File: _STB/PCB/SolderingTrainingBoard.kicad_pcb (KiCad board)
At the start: 2 copper layers, 87.3 x 87.3 mm, 161 parts

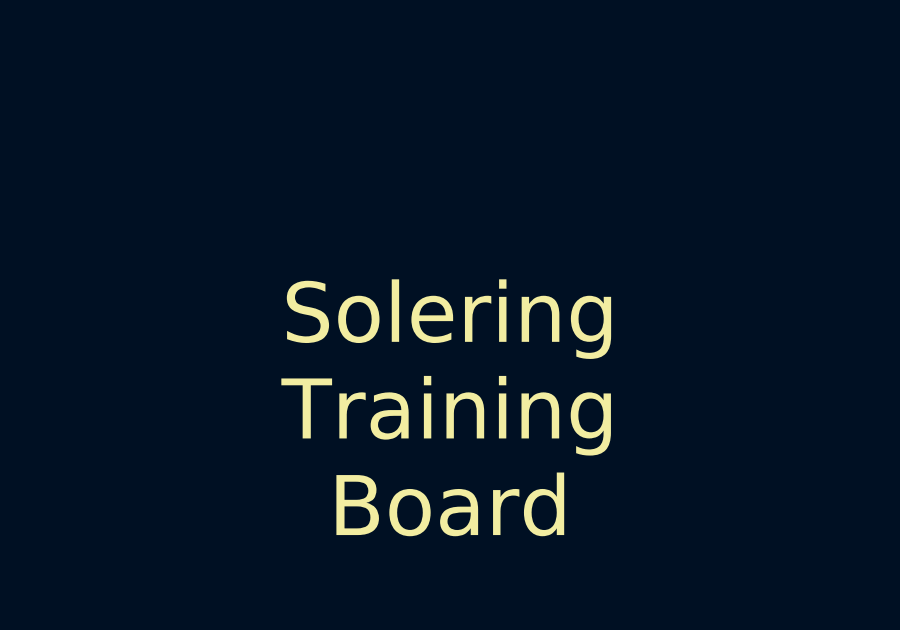
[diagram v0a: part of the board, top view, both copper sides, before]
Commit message: Fix Typo in STB-Silkscreen
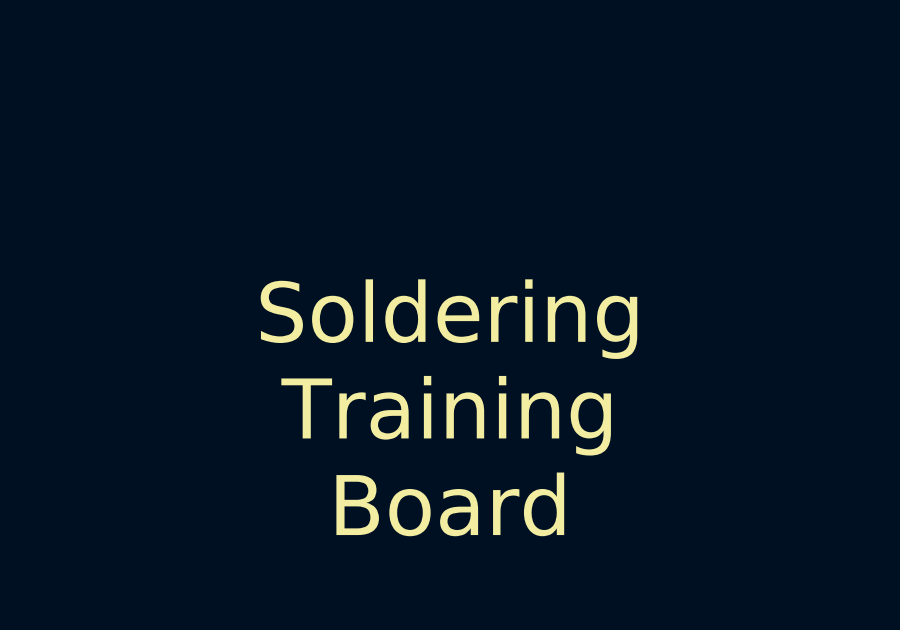
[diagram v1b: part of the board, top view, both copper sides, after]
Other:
- board text added: "Soldering Training Board"
- board text removed: "Solering Training Board"
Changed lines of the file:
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@@
     (effects (font (size 1 1) (thickness 0.15)))
   )
-  (gr_text "Solering\nTraining\nBoard" (at 164.30625 150.8125) (layer F.SilkS)
+  (gr_text "Soldering\nTraining\nBoard" (at 164.30625 150.8125) (layer F.SilkS)
     (effects (font (size 2 2) (thickness 0.15)))
   )
